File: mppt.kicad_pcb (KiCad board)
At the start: 2 copper layers, 50.2 x 49.6 mm, 56 parts, among them P101 CONN_01X02, P102 CONN_01X02, P103 JTAG, P104 CONN_01X02, Q201 IRF7343PBF, U101 ST3485ECDR, U102 STM32F103C8Tx, U201 358, U202 358, U301 lm2575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

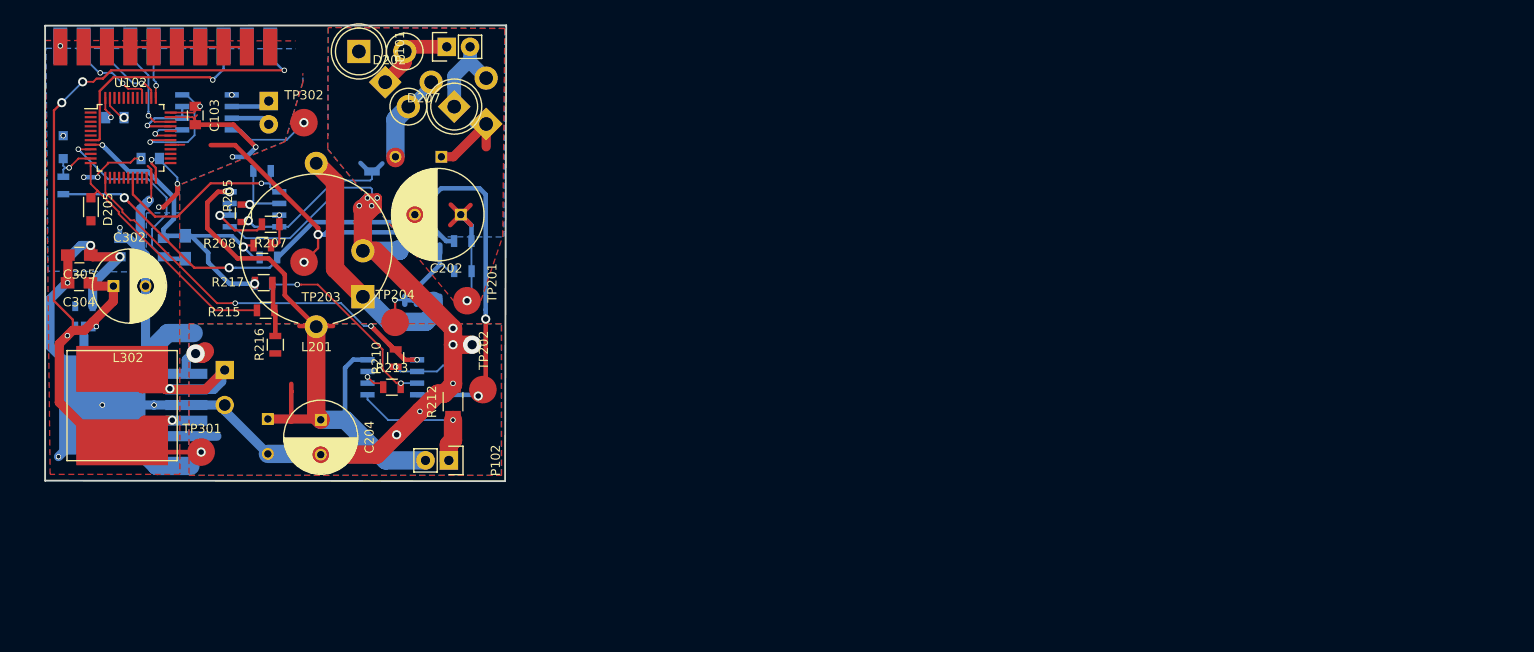
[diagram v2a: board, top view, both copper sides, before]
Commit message: Rerouted, and made everything beautifull
 - added screw bolt-holes for the output.
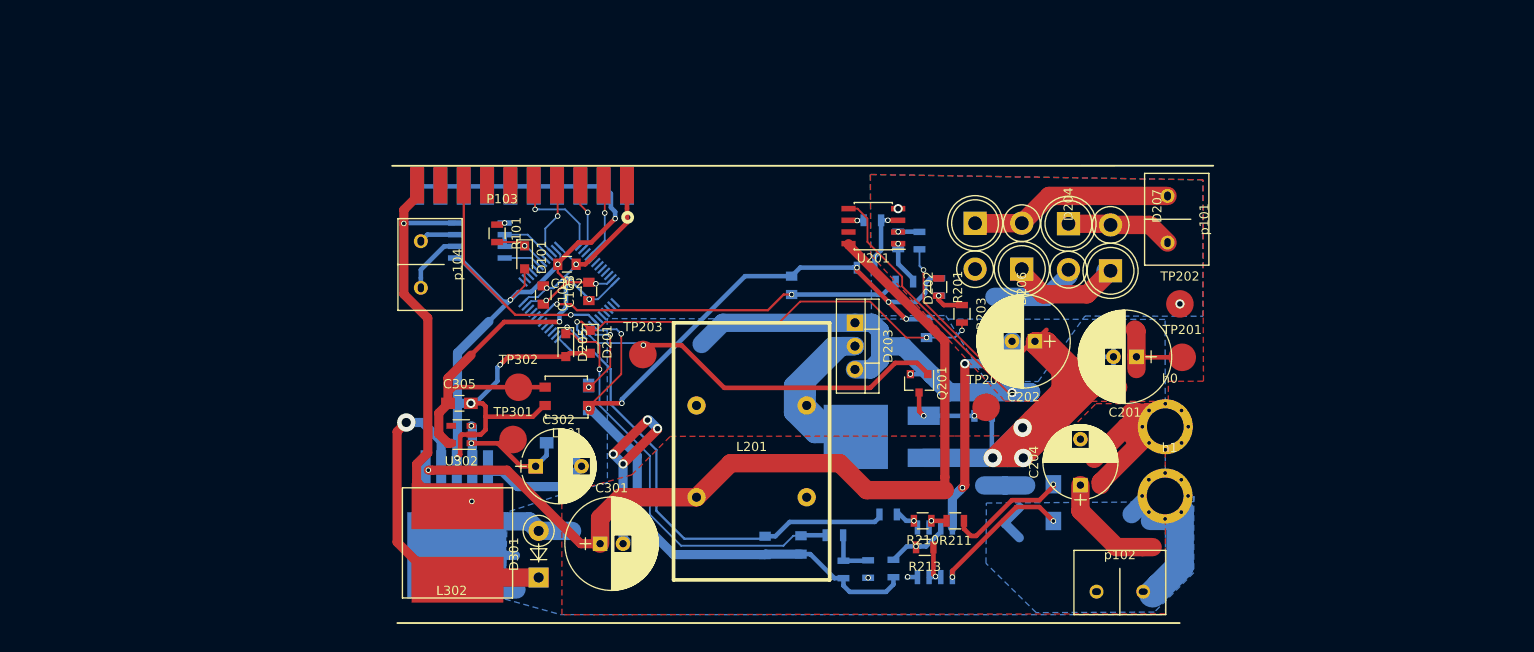
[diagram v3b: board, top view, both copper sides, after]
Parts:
- removed P101, P102, P104: CONN_01X02, Pin_Headers:Pin_Header_Straight_1x02
- added C203: 100nF, Capacitors_SMD:C_0805, B.Cu at (136.0, 73.4)
- added C205: 100nF, Capacitors_SMD:C_0805, B.Cu at (121.3, 68.7)
- added C206: 100nF, Capacitors_SMD:C_0805, B.Cu at (118.4, 97.0)
- added C207: 100nF, Capacitors_SMD:C_0805, B.Cu at (122.3, 97.0)
- added D101: 3v, Diodes_SMD:D_SOD-323_HandSoldering, F.Cu at (92.2, 65.7)
- added Q202: STD35P6LLF6, TO_SOT_Packages_SMD:TO-252-2Lead, B.Cu at (131.9, 85.2)
- added R101: 1k, Resistors_SMD:R_0805, F.Cu at (89.2, 63.1)
- added R218: 10k, Resistors_SMD:R_0805, B.Cu at (133.5, 68.3)
- added R219: 10k, Resistors_SMD:R_0805, B.Cu at (131.8, 93.7)
- added h0: bat+, m4_hole, F.Cu at (162.0, 84.1)
- added h1: bat-, lib:m4_hole, F.Cu at (161.9, 91.7)
- added p101: Screw_Terminal_1x02, lib:terminal, F.Cu at (162.2, 61.5)
- added p102: Screw_Terminal_1x02, lib:terminal, F.Cu at (157.0, 102.1)
- added p104: Screw_Terminal_1x02, lib:terminal, F.Cu at (80.9, 66.4)
- C101, C102, D204, D206, L301, P103, R201, R203, R211, U201, U302: moved to F.Cu
- C201: footprint Capacitors_ThroughHole:C_Radial_D10_L16_P5 -> Capacitors_ThroughHole:CP_Radial_D10.0mm_P2.50mm; moved to F.Cu
- C202: footprint Capacitors_ThroughHole:C_Radial_D10_L16_P5 -> Capacitors_ThroughHole:CP_Radial_D10.0mm_P2.50mm
- C204: footprint Capacitors_ThroughHole:C_Radial_D8_L21_P3.8 -> Capacitors_ThroughHole:CP_Radial_D8.0mm_P5.00mm
- C301: footprint Capacitors_ThroughHole:C_Radial_D8_L21_P3.8 -> Capacitors_ThroughHole:CP_Radial_D10.0mm_P2.50mm; moved to F.Cu
- C302: footprint Capacitors_ThroughHole:C_Radial_D8_L11.5_P3.5 -> Capacitors_ThroughHole:CP_Radial_D8.0mm_P5.00mm
- C304, R205, R207, R208, R212, R215, R216, R217: moved to B.Cu
- D201: footprint Diodes_SMD:SOD-323_HandSoldering -> Diodes_SMD:D_SOD-323_HandSoldering; moved to F.Cu
- D203: value D_Schottky -> STPS10H100C; footprint lib:Diode_DO-201AD_Vertical -> TO_SOT_Packages_THT:TO-220_Vertical; moved to F.Cu
- D205: footprint Diodes_SMD:SOD-323_HandSoldering -> Diodes_SMD:D_SOD-323_HandSoldering
- D301: footprint Diodes_ThroughHole:Diode_DO-41_SOD81_Vertical_KathodeUp -> Diodes_ThroughHole:D_DO-41_SOD81_P5.08mm_Vertical_KathodeUp; moved to F.Cu
- L201: footprint PCV-0-104-05L -> lib:toroid
- Q201: value IRF7343PBF -> 2n7002; footprint Power_Integrations:SO-8 -> TO_SOT_Packages_SMD:SOT-23; moved to F.Cu
- R209: value R -> 1k
- U102: value STM32F103C8Tx -> STM32F103CBTx; moved to B.Cu
- moved R203 98.9 mm to (139.8, 71.8), turned to 270 degrees
- moved D207 85.3 mm to (156.0, 67.1), turned to 90 degrees
- moved C204 83.1 mm to (152.7, 90.5), turned to 90 degrees
- moved C201 78.8 mm to (158.8, 76.5)
- moved TP201 78.1 mm to (163.8, 76.6)
- moved TP202 76.5 mm to (163.6, 70.7)
- moved D206 76.0 mm to (151.4, 62.0), turned to 270 degrees
- moved R214 75.3 mm to (132.3, 99.6), turned to 270 degrees
- moved R205 73.7 mm to (135.2, 63.8)
- moved R202 73.1 mm to (137.3, 68.9), turned to 90 degrees
- moved R206 72.9 mm to (145.3, 79.0)
- moved R217 70.5 mm to (126.9, 99.7), turned to 270 degrees
- moved R204 69.7 mm to (132.9, 63.8), turned to 270 degrees
- moved R216 69.0 mm to (129.6, 99.6)
- moved U201 67.4 mm to (130.2, 62.3)
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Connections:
- C201 pad 2: /regulator/in_rect- -> GND
- D203 pad 1: Net-(D203-Pad1) -> GND
- D203 pad 2: GND -> /regulator/switchpool
- L201 pad 1: Net-(D203-Pad1) -> /regulator/switchpool
- Q201 pad 1: GND -> /REGUL_PULSE
- Q201 pad 2: /REGUL_PULSE -> GND
- Q201 pad 3: /regulator/in_rect+ -> Net-(Q201-Pad3)
- R204 pad 2: /Iin -> Net-(R204-Pad2)
- R209 pad 2: Net-(Q201-Pad4) -> Net-(Q201-Pad3)
- R210 pad 2: /regulator/Iout -> Net-(R210-Pad2)
- TP204 pad 1: Net-(Q201-Pad4) -> Net-(Q201-Pad3)
- U101 pad 1: /nmeaRX -> Net-(R101-Pad1)
- U101 pad 8: +3V3 -> +5V
- U102 pad 10: (no net) -> /REGUL_PULSE
- U102 pad 29: /REGUL_PULSE -> (no net)
- U201 pad 1: /Iin -> Net-(R204-Pad2)
- U202 pad 1: /regulator/Iout -> Net-(R210-Pad2)
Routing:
- net /regulator/in_rect+: track 29.1 -> 108.3 mm, vias 4 -> 3
- net GNDA: track 40.1 -> 113.4 mm, vias 3 -> 6
- net +24V: track 73.1 -> 138.1 mm, vias 2 -> 3
- net GND: track 277.7 -> 324.8 mm, vias 24 -> 15
- net Net-(R201-Pad2): track 48.9 -> 3.23 mm, vias 2 -> 1
- net /regulator/Uin: track 5.78 -> 48.1 mm, vias 1 -> 3
- net /regulator/switchpool: track 0.00 -> 35.7 mm
- net +3V3: track 39.6 -> 73.5 mm, vias 9 -> 4
- net Net-(D203-Pad1): track 28.6 -> 0.00 mm
- net +5V: track 100.3 -> 72.0 mm, vias 7 -> 4
- net /regulator/BATTERY-: track 15.3 -> 41.2 mm, vias 1 -> 2
- net /regulator/Ubat: track 27.3 -> 48.6 mm, vias 0 -> 2
- net /Iin: track 22.3 -> 41.1 mm, vias 1 -> 2
- net /regulator/in_rect-: track 73.6 -> 55.4 mm, vias 3 -> 6
- net /regulator/GENERATOR_IN+: track 10.5 -> 25.5 mm
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- added copper zone on B.Cu, net /regulator/BATTERY-
- removed copper zone on B.Cu, net +3V3
- removed copper zone on F.Cu, net GND
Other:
- board outline removed

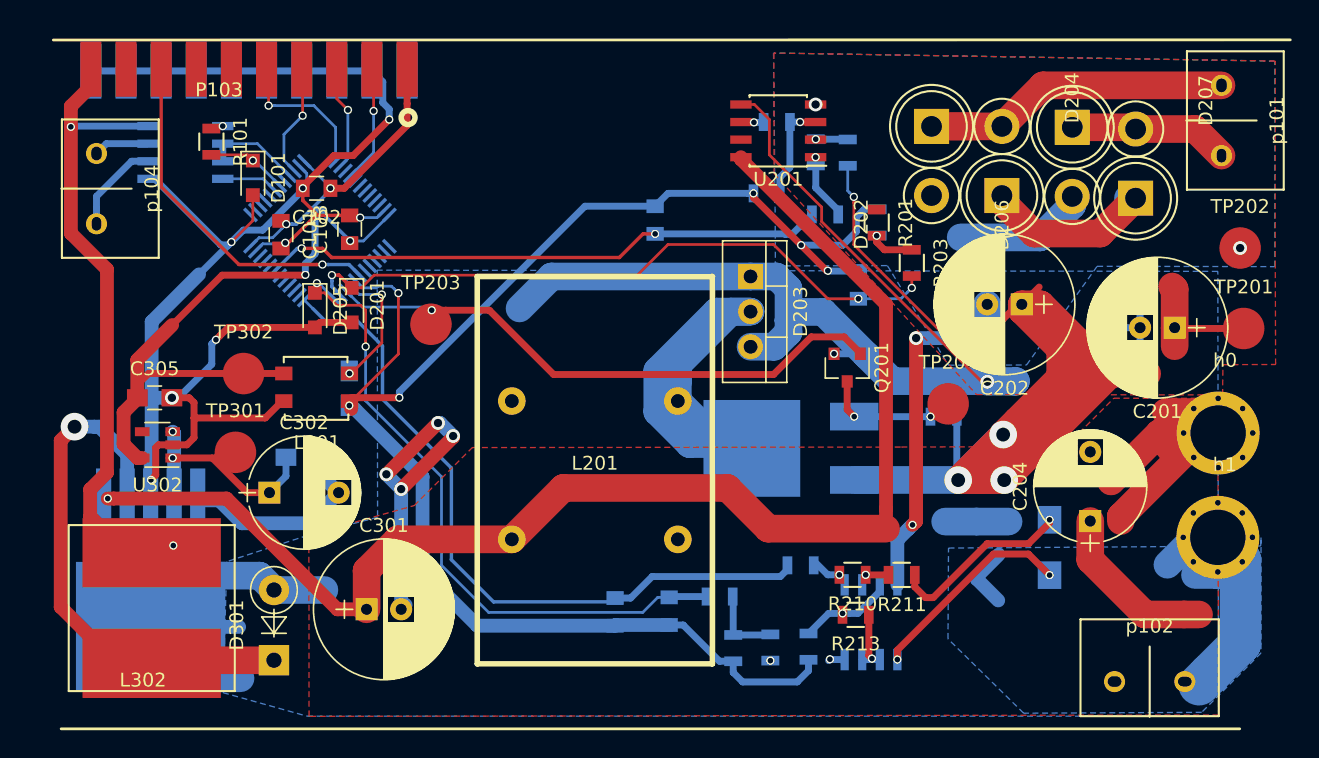
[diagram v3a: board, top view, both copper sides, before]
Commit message: Added small display.
And made everything look even nicer
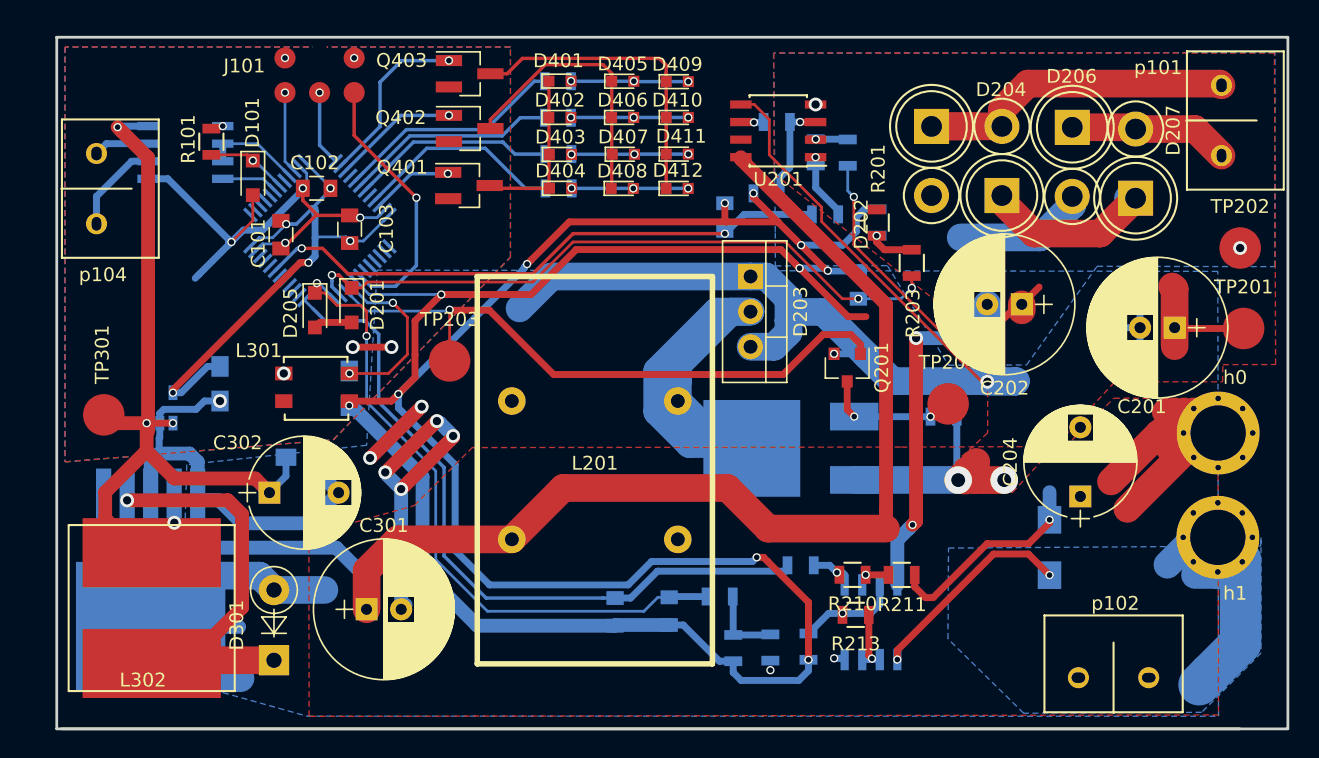
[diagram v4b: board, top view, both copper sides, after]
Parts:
- removed P103: JTAG, lib:20p_edge
- removed TP302: TEST, Measurement_Points:Measurement_Point_Round-SMD-Pad_Big
- added D401: LED, LEDs:LED_0603, F.Cu at (114.4, 58.7)
- added D402: LED, LEDs:LED_0603, F.Cu at (114.4, 61.3)
- added D403: LED, LEDs:LED_0603, F.Cu at (114.4, 64.0)
- added D404: LED, LEDs:LED_0603, F.Cu at (114.4, 66.4)
- added D405: LED, LEDs:LED_0603, F.Cu at (118.9, 58.7)
- added D406: LED, LEDs:LED_0603, F.Cu at (118.9, 61.3)
- added D407: LED, LEDs:LED_0603, F.Cu at (119.0, 64.0)
- added D408: LED, LEDs:LED_0603, F.Cu at (118.9, 66.4)
- added D409: LED, LEDs:LED_0603, F.Cu at (122.9, 58.7)
- added D410: LED, LEDs:LED_0603, F.Cu at (122.9, 61.3)
- added D411: LED, LEDs:LED_0603, F.Cu at (122.9, 64.0)
- added D412: LED, LEDs:LED_0603, F.Cu at (122.8, 66.4)
- added J101: CONN_01X05, swd_conn, F.Cu at (97.0, 57.5)
- added Q401: Q_NMOS_GSD, TO_SOT_Packages_SMD:SOT-23_Handsoldering, F.Cu at (107.8, 66.2)
- added Q402: Q_NMOS_GSD, TO_SOT_Packages_SMD:SOT-23_Handsoldering, F.Cu at (107.8, 62.1)
- added Q403: Q_NMOS_GSD, TO_SOT_Packages_SMD:SOT-23_Handsoldering, F.Cu at (107.8, 58.1)
- added R409: 1k, Resistors_SMD:R_0805, B.Cu at (114.2, 58.7)
- added R410: 1k, Resistors_SMD:R_0805, B.Cu at (114.2, 61.3)
- added R411: 1k, Resistors_SMD:R_0805, B.Cu at (114.3, 64.0)
- added R412: 1k, Resistors_SMD:R_0805, B.Cu at (114.3, 66.4)
- C305, U302: moved to B.Cu
- moved TP301 9.90 mm to (81.4, 82.8)
- moved C205 5.05 mm to (126.3, 68.5)
- moved C305 4.83 mm to (89.8, 80.5), turned to 270 degrees
- moved TP203 2.97 mm to (106.4, 78.9)
- moved U302 2.67 mm to (85.5, 82.3), turned to 90 degrees
- moved p102 2.63 mm to (154.4, 101.8)
- moved C204 1.91 mm to (152.0, 88.7)
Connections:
- U102 pad 34: /jtms -> /swdio
- U102 pad 37: /jtck -> /swclk
- U102 pad 38: /jtdi -> /leds/inC
- U102 pad 39: (no net) -> /leds/inB
- U102 pad 40: /jnrst -> (no net)
- U102 pad 41: (no net) -> /leds/in1
- U102 pad 42: (no net) -> /leds/in2
- U102 pad 43: (no net) -> /leds/in3
- U102 pad 45: (no net) -> /leds/in4
- U102 pad 46: (no net) -> /leds/inA
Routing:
- net GNDA: track 113.4 -> 200.5 mm, vias 6 -> 11
- net GND: track 324.8 -> 242.3 mm
- net /regulator/in_rect+: track 108.3 -> 44.2 mm, vias 3 -> 2
- net +3V3: track 73.5 -> 39.9 mm, vias 4 -> 7
- net Net-(D409-Pad1): track 0.00 -> 22.3 mm
- net Net-(D405-Pad1): track 0.00 -> 19.7 mm
- net /leds/in1: track 0.00 -> 16.7 mm
- net /leds/in2: track 0.00 -> 15.4 mm
- net /leds/in4: track 0.00 -> 15.1 mm
- net /leds/in3: track 0.00 -> 14.8 mm
- net /leds/inC: track 0.00 -> 12.9 mm, vias 0 -> 1
- net Net-(D401-Pad1): track 0.00 -> 12.2 mm
- net /jtck: track 10.6 -> 0.00 mm, vias 1 -> 0
- net +24V: track 138.1 -> 128.0 mm, vias 3 -> 1
- net +5V: track 72.0 -> 62.7 mm
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- added copper zone on B.Cu, net +3V3
- added copper zone on F.Cu, net GND
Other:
- board outline added: 89 x 50 mm
